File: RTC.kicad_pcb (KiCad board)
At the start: 2 copper layers, 85 x 65 mm, 53 parts, among them J1 Conn_01x01_Socket, J2 Conn_01x01_Socket, X1 Power, X2 Address, X3 Data, X4 Mode, X5 Control, X6 Clock

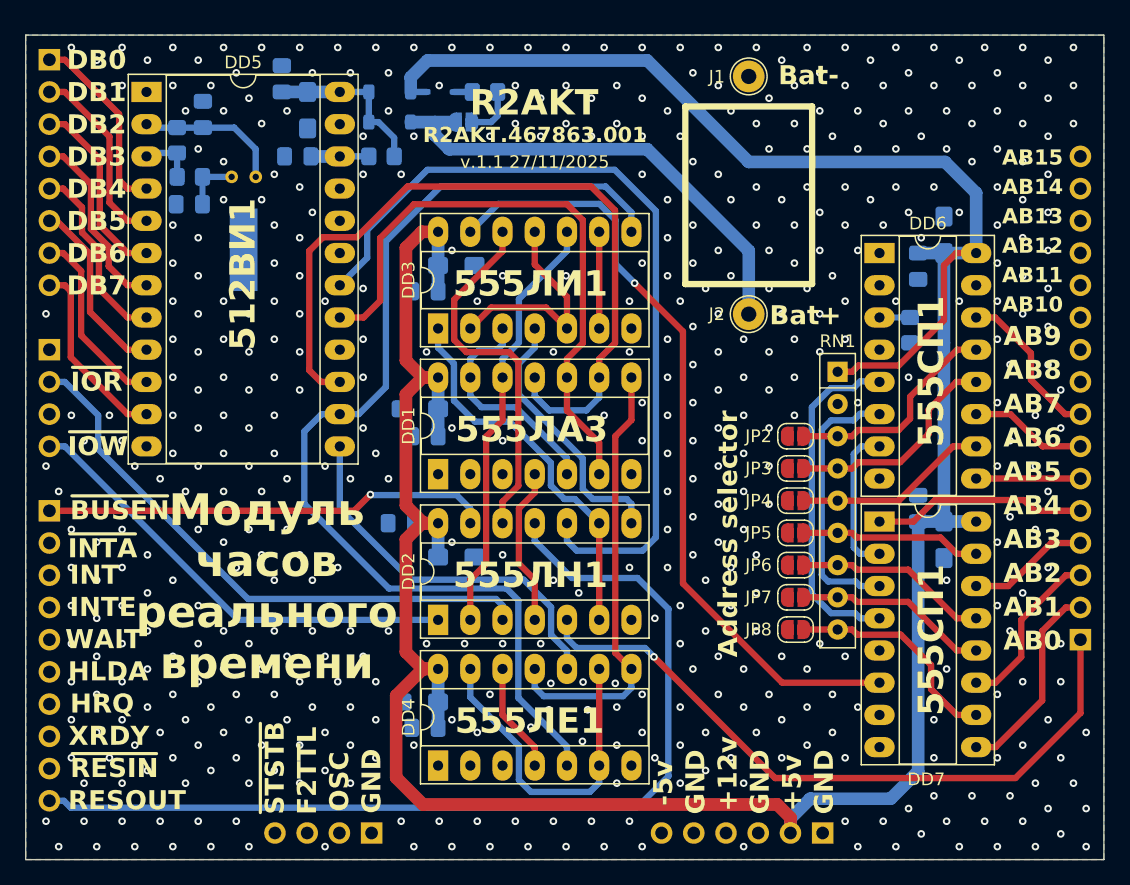
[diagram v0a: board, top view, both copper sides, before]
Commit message: Add files via upload
Changed chip power-up reset schemtic, added IRQ option, fix silk problem.

Изменена схема сброса часов при подаче питания, добавлена опция IRQ, исправлены проблемы с шелкографией.
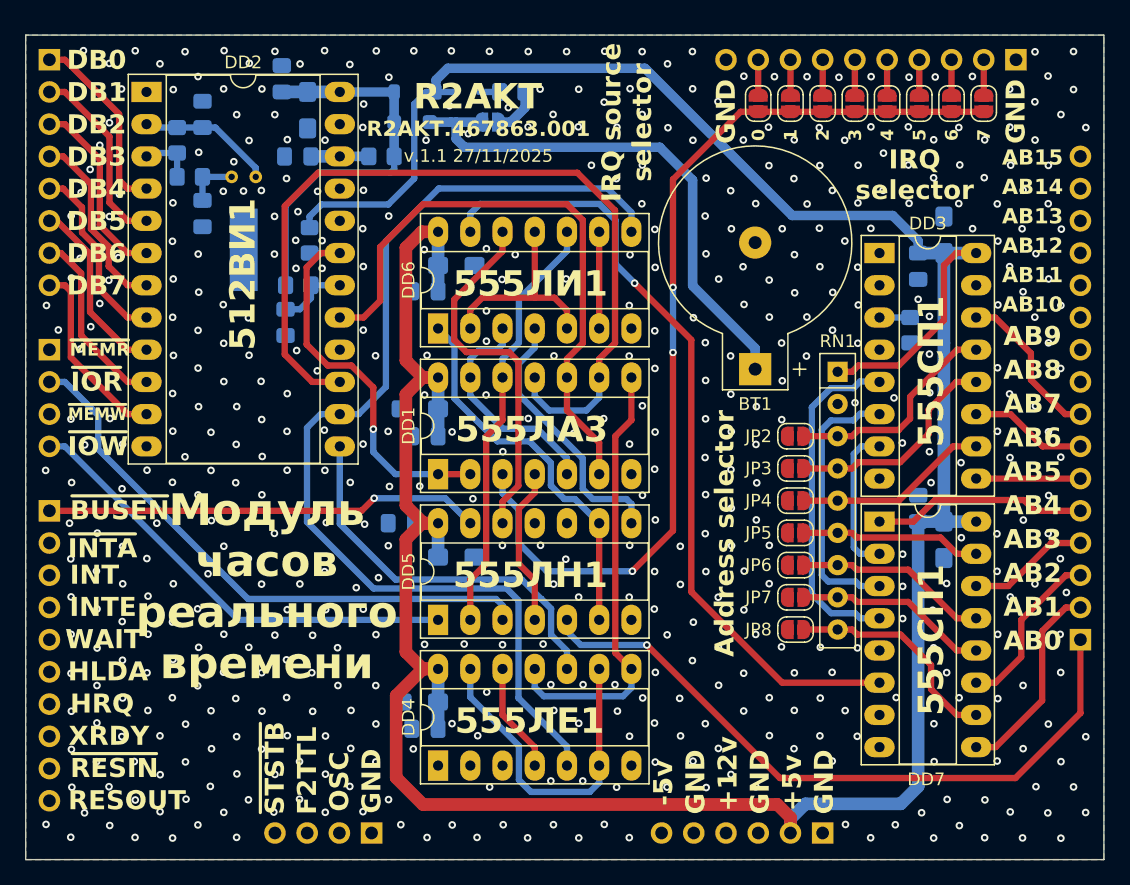
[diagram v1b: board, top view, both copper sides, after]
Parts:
- removed J1, J2: Conn_01x01_Socket, TestPoint:TestPoint_THTPad_D2.5mm_Drill1.2mm
- added BT1: Battery, Battery:BatteryHolder_Keystone_500, F.Cu at (124.9, 113.0)
- added C2: 6n8, Capacitor_SMD:C_0805_2012Metric_Pad1.18x1.45mm_HandSolder, B.Cu at (87.9, 109.3)
- added JP10: IRQ1, Jumper:SolderJumper-2_P1.3mm_Open_RoundedPad1.0x1.5mm, F.Cu at (127.7, 92.1)
- added JP11: IRQ2, Jumper:SolderJumper-2_P1.3mm_Open_RoundedPad1.0x1.5mm, F.Cu at (130.2, 92.1)
- added JP12: IRQ3, Jumper:SolderJumper-2_P1.3mm_Open_RoundedPad1.0x1.5mm, F.Cu at (132.8, 92.1)
- added JP13: IRQ4, Jumper:SolderJumper-2_P1.3mm_Open_RoundedPad1.0x1.5mm, F.Cu at (135.3, 92.1)
- added JP14: IRQ5, Jumper:SolderJumper-2_P1.3mm_Open_RoundedPad1.0x1.5mm, F.Cu at (137.9, 92.1)
- added JP15: IRQ6, Jumper:SolderJumper-2_P1.3mm_Open_RoundedPad1.0x1.5mm, F.Cu at (140.4, 92.1)
- added JP16: IRQ7, Jumper:SolderJumper-2_P1.3mm_Open_RoundedPad1.0x1.5mm, F.Cu at (142.9, 92.1)
- added JP9: IRQ0, Jumper:SolderJumper-2_P1.3mm_Open_RoundedPad1.0x1.5mm, F.Cu at (125.2, 92.1)
- added R1: 1k, Resistor_SMD:R_0805_2012Metric_Pad1.20x1.40mm_HandSolder, B.Cu at (89.8, 102.9)
- added R3: 20k, Resistor_SMD:R_0805_2012Metric_Pad1.20x1.40mm_HandSolder, B.Cu at (88.9, 106.4)
- added X7: Conn_01x10, Connector_PinHeader_2.54mm:PinHeader_1x10_P2.54mm_Vertical, B.Cu at (145.5, 88.6)
- D1: renamed from D2; footprint Diode_SMD:D_SOD-123 -> Diode_SMD:D_SOD-123F
- R4: renamed from R2; value 22M -> 10M
- moved REF** 4.59 mm to (125.0, 108.0)
- moved R6 2.15 mm to (105.8, 91.2)
- moved D3 2.08 mm to (102.2, 91.2)
- moved JP1 2.08 mm to (104.0, 93.5)
- moved D2 2.00 mm to (98.1, 91.2)
- moved D1 1.75 mm to (97.9, 93.5)
- moved C6 1.27 mm to (81.3, 100.7), turned to 90 degrees
- moved REF** 1.12 mm to (124.1, 124.8), turned to 90 degrees
- moved C13 0.08 mm to (98.9, 141.4)
- renumbered C11 to C1, C17 to C10, C1 to C11, C3 to C12, C7 to C13, C12 to C14, C2 to C15, C4 to C16, C8 to C17, C13 to C18, C5 to C3, C14 to C4, C15 to C5, C9 to C7, C10 to C8, C16 to C9, D1 to D2, DD5 to DD2, DD6 to DD3, DD2 to DD5, DD3 to DD6, R3 to R2, R1 to R5, R4 to R6, R5 to R7
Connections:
- DD1 pad 1: GND -> Net-(DD2-~{IRQ})
- DD1 pad 2: GND -> Net-(DD2-~{IRQ})
- DD1 pad 3: unconnected-(DD1-Pad3) -> /IRQ_RTC
- DD2 pad 18: /~{RTC_RESET} -> Net-(DD2-~{RST})
- DD2 pad 19: unconnected-(DD5-~{IRQ}-Pad19) -> Net-(DD2-~{IRQ})
- DD5 pad 10: /~{RTC_RESET} -> unconnected-(DD5-Pad10)
- DD5 pad 11: /RESOUT -> GND
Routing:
- net /RESOUT: track 77.4 -> 0.00 mm
- net /IRQ_RTC: track 0.00 -> 74.8 mm, vias 0 -> 3
- net /~{RTC_RESET}: track 66.2 -> 0.00 mm
- net Net-(DD2-~{IRQ}): track 0.00 -> 31.7 mm, vias 0 -> 1
- net Net-(D1-K): track 13.2 -> 31.0 mm
- net +5: track 247.2 -> 256.9 mm
- net /RTC_R/~{W}: track 61.9 -> 68.0 mm
- net Net-(DD2-~{RST}): track 0.00 -> 5.66 mm
- net Net-(BT1-+): track 38.1 -> 42.4 mm
- net /IRQ7: track 0.00 -> 2.80 mm
- net /IRQ6: track 0.00 -> 2.80 mm
- net /IRQ5: track 0.00 -> 2.80 mm
- net /IRQ4: track 0.00 -> 2.80 mm
- net /IRQ3: track 0.00 -> 2.80 mm
- net /IRQ2: track 0.00 -> 2.80 mm
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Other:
- board text added: "0"
- board text added: "1"
- board text added: "3"
- board text added: "4"
- board text added: "5"
- board text added: "6"
- board text added: "7"
- board text added: "IRQ selector"
- board text added: "IRQ source selector"
- board text added: "IRQ0"
- board text added: "IRQ1"
- board text added: "IRQ2"
- board text added: "IRQ3"
- board text added: "IRQ4"
- board text added: "IRQ5"
- board text added: "IRQ6"
- board text added: "IRQ7"
- board text added: "~{MEMR}"
- board text added: "~{MEMW}"
- board text removed: "Bat+"
- board text removed: "Bat-"

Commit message: Add files via upload
Fix start-up reset issue

Устранение проблемы начального сброса
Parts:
- C2: value 6n8 -> 4n7
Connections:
- R3 pad 1: Net-(D1-K) -> +5
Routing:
- net Net-(D1-K): track 31.0 -> 13.9 mm
- net +5: track 256.9 -> 262.9 mm
- net GND: vias 531 -> 536
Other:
- board text added: "v.1.2 11/03/2026"
- board text removed: "v.1.1 27/11/2025"

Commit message: Add files via upload
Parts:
- added C9: 100n, Capacitor_SMD:C_0805_2012Metric_Pad1.18x1.45mm_HandSolder, B.Cu at (131.4, 108.9)
- added D1: 1N4148WS, Diode_SMD:D_SOD-323_HandSoldering, B.Cu at (95.7, 98.2)
- added D2: 1N4148WS, Diode_SMD:D_SOD-323_HandSoldering, B.Cu at (94.6, 105.1)
- added D4: 1N4148WS, Diode_SMD:D_SOD-323_HandSoldering, B.Cu at (124.9, 117.2)
- added JP1: Btr. PWR, Jumper:SolderJumper-2_P1.3mm_Open_RoundedPad1.0x1.5mm, B.Cu at (124.9, 125.1)
- added R4: 1k, Resistor_SMD:R_0805_2012Metric_Pad1.20x1.40mm_HandSolder, B.Cu at (124.9, 121.3)
- added X8: RTC Standby, Connector_PinHeader_2.54mm:PinHeader_1x02_P2.54mm_Vertical, B.Cu at (140.4, 149.6)
- C1, C2: value 4n7 -> 6n8
- D6: renamed from D3; footprint Diode_SMD:D_SOD-323 -> Diode_SMD:D_SOD-323_HandSoldering
- R2: value 20k -> 10k
- R3: value 20k -> 1k
- moved REF** 38.8 mm to (85.4, 127.5)
- moved REF** 38.5 mm to (124.1, 135.0)
- moved R7 0.85 mm to (106.6, 91.2)
- moved D6 0.42 mm to (102.6, 91.2)
- turned JP2 to 180 degrees
- renumbered C9 to C10, C10 to C11, C11 to C12, C12 to C13, C13 to C14, C14 to C15, C15 to C16, C16 to C17, C17 to C18, C18 to C19, D1 to D3, D2 to D5, JP9 to JP10, JP10 to JP11, JP11 to JP12, JP12 to JP13, JP13 to JP14, JP14 to JP15, JP15 to JP16, JP16 to JP17, JP1 to JP2, JP2 to JP3, JP3 to JP4, JP4 to JP5, JP5 to JP6, JP6 to JP7, JP7 to JP8, JP8 to JP9, R4 to R5, R5 to R6, R6 to R7, R7 to R8
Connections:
- net /INTE renamed /~{WRQ}
- net /Single_BCLK renamed /F2TTL
- net /Single_OSC_TTL renamed /OSC_TTL
- JP2 pad 1: Net-(BT1-+) -> Net-(JP2-A)
- JP2 pad 2: Net-(JP1-B) -> Net-(BT1-+)
- R7 pad 2: Net-(JP1-B) -> Net-(JP2-A)
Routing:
- net /+5VSB: track 0.00 -> 31.8 mm, vias 0 -> 2
- net Net-(JP2-A): track 0.00 -> 4.57 mm
- net Net-(JP1-B): track 3.81 -> 0.00 mm
- net Net-(BT1-+): track 42.4 -> 45.3 mm
- net Net-(D4-A): track 0.00 -> 2.46 mm
- net Net-(D2-A): track 5.66 -> 8.05 mm
- net Net-(DD3-Ia=b): track 2.41 -> 4.71 mm
- net Net-(D1-K): track 13.9 -> 16.1 mm
- net Net-(JP1-A): track 0.00 -> 2.15 mm
- net Net-(D1-A): track 4.57 -> 6.57 mm
- net +5: track 262.9 -> 264.7 mm
- net /RTC_R/~{W}: track 68.0 -> 66.7 mm
- net /AB0: track 54.1 -> 53.6 mm
- net GND: vias 536 -> 521
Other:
- board text added: "+5VSB"
- board text added: "~{WRQ}"
- board text removed: "INTE"
- board text removed: "IRQ source selector"
